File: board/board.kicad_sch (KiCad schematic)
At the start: 3 parts, among them J1 001_I2C, J2 011_GPIO

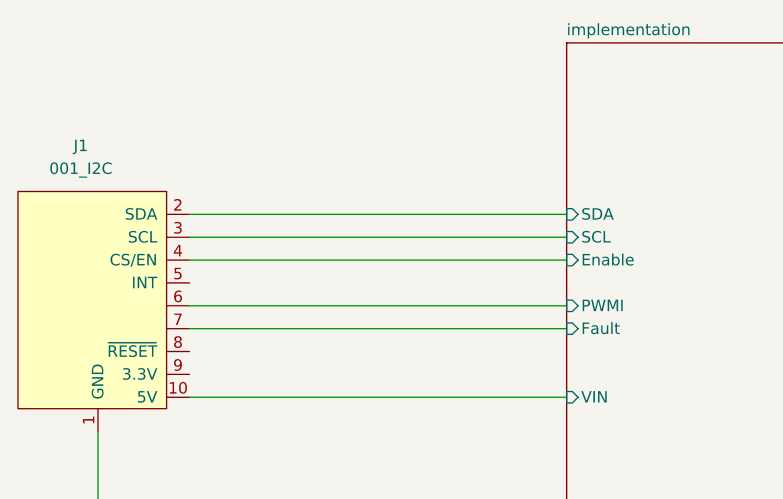
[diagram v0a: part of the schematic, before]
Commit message: Add Testpoint | Add relative footrpint/symbol path
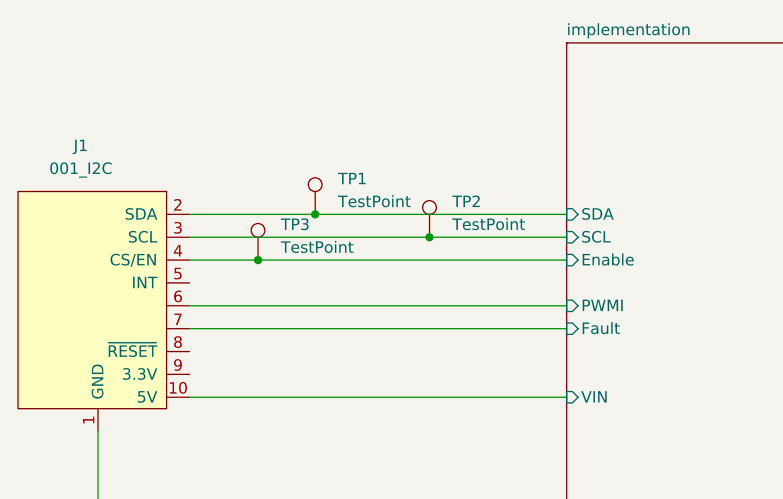
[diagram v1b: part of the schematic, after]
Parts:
- added TP1, TP2, TP3: TestPoint, TestPoint:TestPoint_Pad_D1.0mm, symbol Connector:TestPoint
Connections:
- net implementation/Enable: now also TP3.1
- net implementation/SCL: now also TP2.1
- net implementation/SDA: now also TP1.1
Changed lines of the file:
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@@
   (junction (at 182.88 138.43) (diameter 0) (color 0 0 0 0)
   )
+  (junction (at 86.36 91.44) (diameter 0) (color 0 0 0 0)
+  )
   (junction (at 234.95 113.03) (diameter 0) (color 0 0 0 0)
   )
+  (junction (at 99.06 93.98) (diameter 0) (color 0 0 0 0)
+  )
+  (junction (at 80.01 96.52) (diameter 0) (color 0 0 0 0)
+  )
   (wire (pts (xy 218.44 95.25) (xy 218.44 92.71))
     (stroke (width 0) (type default))
@@
     (stroke (width 0) (type default))
   )
-  (wire (pts (xy 72.39 91.44) (xy 114.3 91.44))
+  (wire (pts (xy 72.39 91.44) (xy 86.36 91.44))
     (stroke (width 0) (type default))
   )
@@
     (stroke (width 0) (type default))
   )
+  (wire (pts (xy 80.01 96.52) (xy 114.3 96.52))
+    (stroke (width 0) (type default))
+  )
   (wire (pts (xy 182.88 138.43) (xy 234.95 138.43))
     (stroke (width 0) (type default))
@@
     (stroke (width 0) (type default))
   )
+  (wire (pts (xy 86.36 91.44) (xy 114.3 91.44))
+    (stroke (width 0) (type default))
+  )
   (wire (pts (xy 189.23 90.17) (xy 189.23 97.79))
     (stroke (width 0) (type default))
@@
     (stroke (width 0) (type default))
   )
+  (wire (pts (xy 99.06 93.98) (xy 114.3 93.98))
+    (stroke (width 0) (type default))
+  )
   (wire (pts (xy 62.23 138.43) (xy 182.88 138.43))
     (stroke (width 0) (type default))
@@
     (stroke (width 0) (type default))
   )
-  (wire (pts (xy 72.39 93.98) (xy 114.3 93.98))
+  (wire (pts (xy 72.39 93.98) (xy 99.06 93.98))
     (stroke (width 0) (type default))
   )
@@
     (stroke (width 0) (type default))
   )
-  (wire (pts (xy 72.39 96.52) (xy 114.3 96.52))
+  (wire (pts (xy 72.39 96.52) (xy 80.01 96.52))
     (stroke (width 0) (type default))
   )
@@
     )
   )
+  (symbol (lib_id "Connector:TestPoint") (at 99.06 93.98 0) (unit 1)
+    (in_bom yes) (on_board yes) (dnp no) (fields_autoplaced)
+    (property "Reference" "TP2" (at 101.6 90.043 0)
+      (effects (font (size 1.27 1.27)) (justify left))
+    )
+    (property "Value" "TestPoint" (at 101.6 92.583 0)
+      (effects (font (size 1.27 1.27)) (justify left))
+    )
+    (property "Footprint" "TestPoint:TestPoint_Pad_D1.0mm" (at 104.14 93.98 0)
+      (effects (font (size 1.27 1.27)) hide)
+    )
+    (property "Datasheet" "~" (at 104.14 93.98 0)
+      (effects (font (size 1.27 1.27)) hide)
+    )
+    (pin "1")
+    (instances
+      (project "board"
+        (path "/57732dd3-1162-4c3f-88bd-31bf473d124d"
+          (reference "TP2") (unit 1)
+        )
+      )
+    )
+  )
+  (symbol (lib_id "Connector:TestPoint") (at 86.36 91.44 0) (unit 1)
+    (in_bom yes) (on_board yes) (dnp no) (fields_autoplaced)
+    (property "Reference" "TP1" (at 88.9 87.503 0)
+      (effects (font (size 1.27 1.27)) (justify left))
+    )
+    (property "Value" "TestPoint" (at 88.9 90.043 0)
+      (effects (font (size 1.27 1.27)) (justify left))
+    )
+    (property "Footprint" "TestPoint:TestPoint_Pad_D1.0mm" (at 91.44 91.44 0)
+      (effects (font (size 1.27 1.27)) hide)
+    )
+    (property "Datasheet" "~" (at 91.44 91.44 0)
+      (effects (font (size 1.27 1.27)) hide)
+    )
+    (pin "1")
+    (instances
+      (project "board"
+        (path "/57732dd3-1162-4c3f-88bd-31bf473d124d"
+          (reference "TP1") (unit 1)
+        )
+      )
+    )
+  )
   (symbol (lib_id "power:GND") (at 182.88 139.7 0) (unit 1)
     (in_bom yes) (on_board yes) (dnp no) (fields_autoplaced)
@@
         )
       )
+    )
+  )
+  (symbol (lib_id "Connector:TestPoint") (at 80.01 96.52 0) (unit 1)
+    (in_bom yes) (on_board yes) (dnp no) (fields_autoplaced)
+    (property "Reference" "TP3" (at 82.55 92.583 0)
+      (effects (font (size 1.27 1.27)) (justify left))
+    )
+    (property "Value" "TestPoint" (at 82.55 95.123 0)
+      (effects (font (size 1.27 1.27)) (justify left))
+    )
+    (property "Footprint" "TestPoint:TestPoint_Pad_D1.0mm" (at 85.09 96.52 0)
+      (effects (font (size 1.27 1.27)) hide)
+    )
+    (property "Datasheet" "~" (at 85.09 96.52 0)
+      (effects (font (size 1.27 1.27)) hide)
+    )
+    (pin "1")
+    (instances
+      (project "board"
+        (path "/57732dd3-1162-4c3f-88bd-31bf473d124d"
+          (reference "TP3") (unit 1)
+        )
+      )
